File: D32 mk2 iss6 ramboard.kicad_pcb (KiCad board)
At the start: 2 copper layers, 117.5 x 53.3 mm, 34 parts, among them IC1 4116, IC2 4116, IC3 4116, IC36 4116, IC37 4116, IC38 4116, IC39 4116, IC4 4116, IC40 4116, IC41 4116, IC42 4116, IC43 4116, IC5 4116, IC6 4116, IC7 4116, IC8 4116, U1 4164, U10 4164, U11 4164, U12 4164, U13 4164, U14 4164, U15 4164, U16 4164, U2 4164, U3 4164, U4 4164, U5 4164, U6 4164, U7 4164, U8 4164, U9 4164

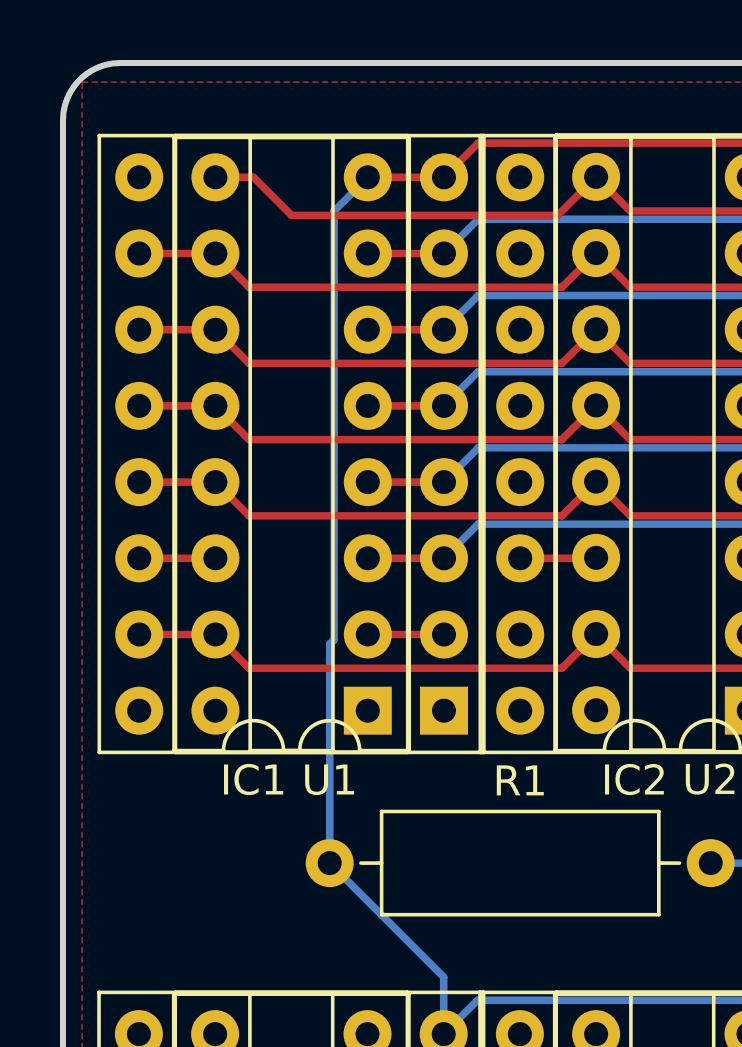
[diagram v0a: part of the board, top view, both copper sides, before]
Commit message: fix 4116 pin bindings
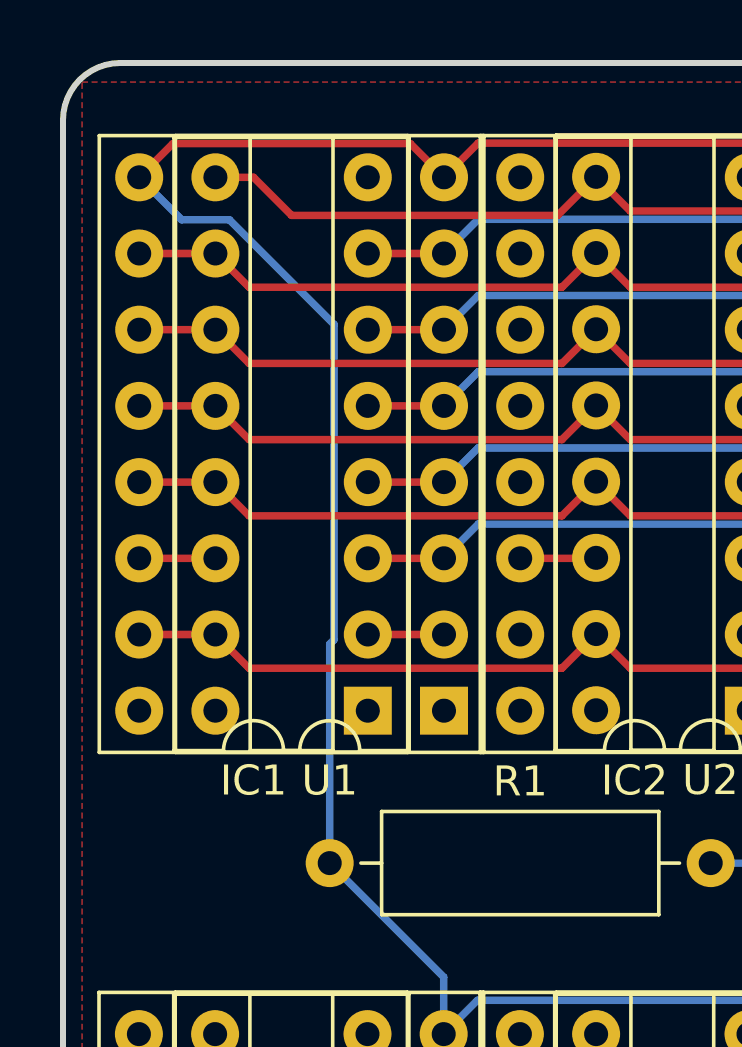
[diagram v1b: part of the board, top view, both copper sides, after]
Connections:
- IC1 pad 8: +5V -> unconnected-(IC1-Pad8)
- IC1 pad 9: unconnected-(IC1-Pad9) -> +5V
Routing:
- net +5V: track 224.2 -> 235.9 mm

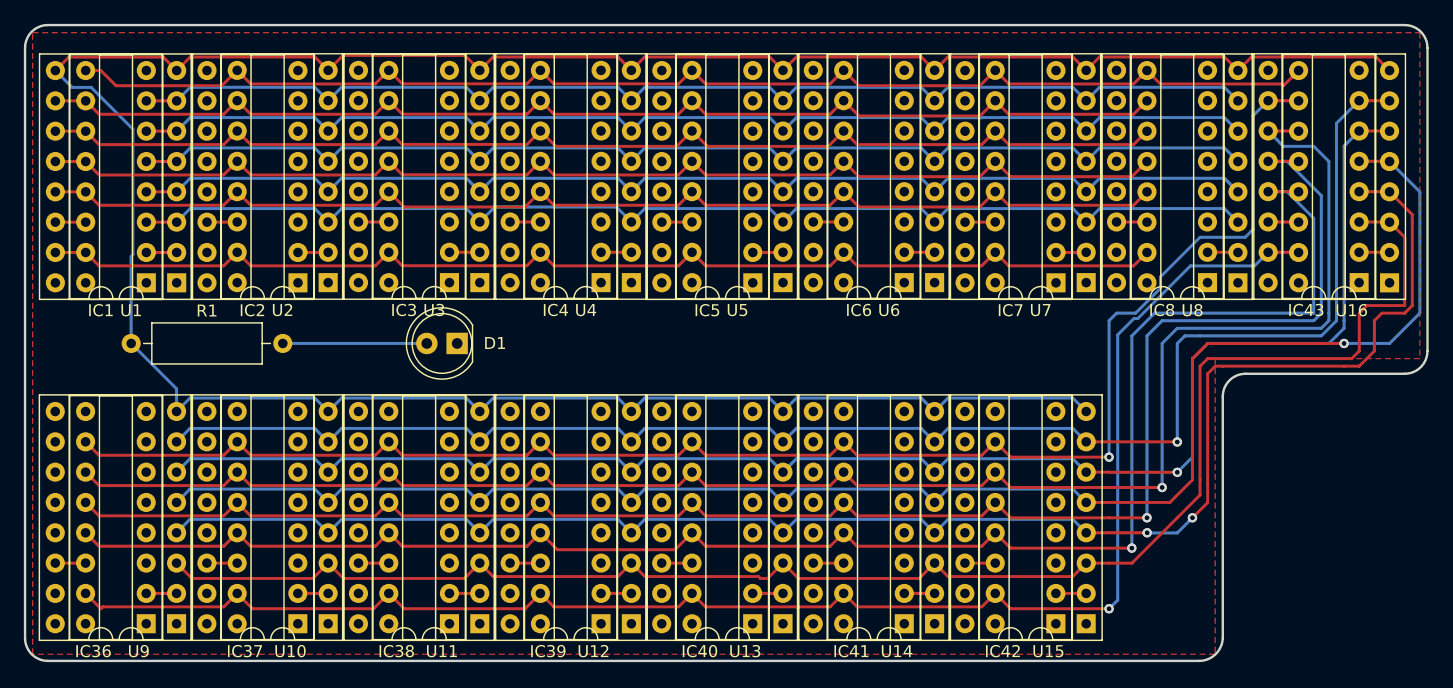
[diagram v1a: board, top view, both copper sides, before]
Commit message: correct 4116 pins and simplify networks
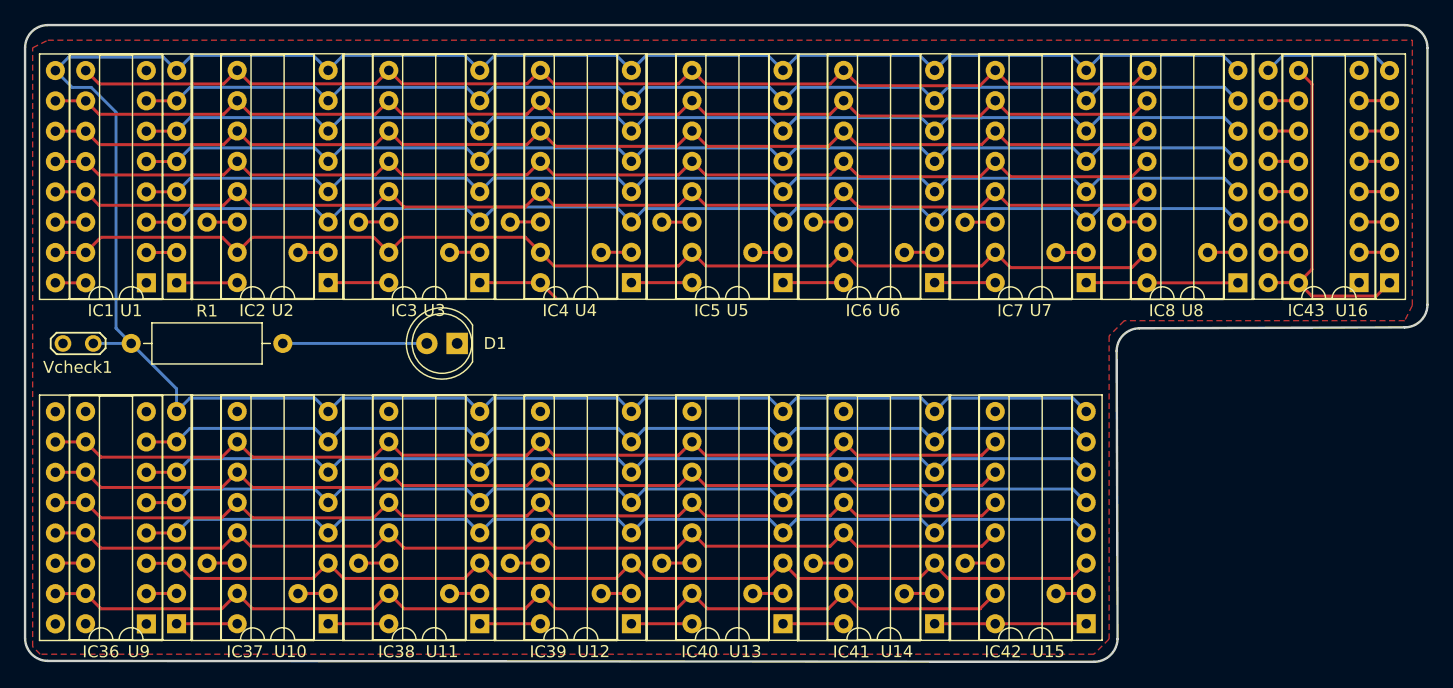
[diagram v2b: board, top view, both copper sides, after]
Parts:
- added Vcheck1: TestPoint_2Pole, TestPoint:TestPoint_2Pads_Pitch2.54mm_Drill0.8mm, F.Cu at (92.1, 91.4)
- IC2, IC3, IC37, IC38, IC39, IC4, IC40, IC41, IC42, IC5, IC6, IC7, IC8: footprint Package_DIP:DIP-16_W7.62mm_Socket -> 4116:4116_Min_DIP-16_W7.62mm_Socket
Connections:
- IC36 pad 10: unconnected-(IC36-Pad10) -> Net-(IC36-Pad10)
- IC36 pad 11: unconnected-(IC36-Pad11) -> Net-(IC36-Pad11)
- IC36 pad 12: unconnected-(IC36-Pad12) -> Net-(IC36-Pad12)
- IC36 pad 13: unconnected-(IC36-Pad13) -> Net-(IC36-Pad13)
- IC36 pad 15: unconnected-(IC36-Pad15) -> Net-(IC36-Pad15)
- IC36 pad 3: unconnected-(IC36-Pad3) -> Net-(IC36-Pad3)
- IC36 pad 4: unconnected-(IC36-Pad4) -> Net-(IC36-Pad4)
- IC36 pad 5: unconnected-(IC36-Pad5) -> Net-(IC36-Pad5)
- IC36 pad 6: unconnected-(IC36-Pad6) -> Net-(IC36-Pad6)
- IC36 pad 7: unconnected-(IC36-Pad7) -> Net-(IC36-Pad7)
- IC43 pad 16: GND -> Net-(IC43-Pad16)
- IC43 pad 9: unconnected-(IC43-Pad9) -> Net-(IC43-Pad9)
- U1 pad 1: unconnected-(U1-Pad1) -> GND
- U10 pad 1: unconnected-(U10-Pad1) -> GND
- U10 pad 10: Net-(IC43-Pad10) -> Net-(IC36-Pad10)
- U10 pad 11: Net-(IC43-Pad11) -> Net-(IC36-Pad11)
- U10 pad 12: Net-(IC43-Pad12) -> Net-(IC36-Pad12)
- U10 pad 13: Net-(IC43-Pad13) -> Net-(IC36-Pad13)
- U10 pad 15: Net-(IC43-Pad15) -> Net-(IC36-Pad15)
- U10 pad 3: Net-(IC43-Pad3) -> Net-(IC36-Pad3)
- U10 pad 4: Net-(IC43-Pad4) -> Net-(IC36-Pad4)
- U10 pad 5: Net-(IC43-Pad5) -> Net-(IC36-Pad5)
- U10 pad 6: Net-(IC43-Pad6) -> Net-(IC36-Pad6)
- U10 pad 7: Net-(IC43-Pad7) -> Net-(IC36-Pad7)
- U11 pad 1: unconnected-(U11-Pad1) -> GND
- U11 pad 10: Net-(IC43-Pad10) -> Net-(IC36-Pad10)
- U11 pad 11: Net-(IC43-Pad11) -> Net-(IC36-Pad11)
- U11 pad 12: Net-(IC43-Pad12) -> Net-(IC36-Pad12)
- U11 pad 13: Net-(IC43-Pad13) -> Net-(IC36-Pad13)
- U11 pad 15: Net-(IC43-Pad15) -> Net-(IC36-Pad15)
- U11 pad 3: Net-(IC43-Pad3) -> Net-(IC36-Pad3)
- U11 pad 4: Net-(IC43-Pad4) -> Net-(IC36-Pad4)
- U11 pad 5: Net-(IC43-Pad5) -> Net-(IC36-Pad5)
- U11 pad 6: Net-(IC43-Pad6) -> Net-(IC36-Pad6)
- U11 pad 7: Net-(IC43-Pad7) -> Net-(IC36-Pad7)
- U12 pad 1: unconnected-(U12-Pad1) -> GND
- U12 pad 10: Net-(IC43-Pad10) -> Net-(IC36-Pad10)
- U12 pad 11: Net-(IC43-Pad11) -> Net-(IC36-Pad11)
- U12 pad 12: Net-(IC43-Pad12) -> Net-(IC36-Pad12)
- U12 pad 13: Net-(IC43-Pad13) -> Net-(IC36-Pad13)
- U12 pad 15: Net-(IC43-Pad15) -> Net-(IC36-Pad15)
- U12 pad 3: Net-(IC43-Pad3) -> Net-(IC36-Pad3)
- U12 pad 4: Net-(IC43-Pad4) -> Net-(IC36-Pad4)
- U12 pad 5: Net-(IC43-Pad5) -> Net-(IC36-Pad5)
- U12 pad 6: Net-(IC43-Pad6) -> Net-(IC36-Pad6)
- U12 pad 7: Net-(IC43-Pad7) -> Net-(IC36-Pad7)
- U13 pad 1: unconnected-(U13-Pad1) -> GND
- U13 pad 10: Net-(IC43-Pad10) -> Net-(IC36-Pad10)
- U13 pad 11: Net-(IC43-Pad11) -> Net-(IC36-Pad11)
- U13 pad 12: Net-(IC43-Pad12) -> Net-(IC36-Pad12)
- U13 pad 13: Net-(IC43-Pad13) -> Net-(IC36-Pad13)
- U13 pad 15: Net-(IC43-Pad15) -> Net-(IC36-Pad15)
- U13 pad 3: Net-(IC43-Pad3) -> Net-(IC36-Pad3)
- U13 pad 4: Net-(IC43-Pad4) -> Net-(IC36-Pad4)
- U13 pad 5: Net-(IC43-Pad5) -> Net-(IC36-Pad5)
- U13 pad 6: Net-(IC43-Pad6) -> Net-(IC36-Pad6)
- U13 pad 7: Net-(IC43-Pad7) -> Net-(IC36-Pad7)
- U14 pad 1: unconnected-(U14-Pad1) -> GND
- U14 pad 10: Net-(IC43-Pad10) -> Net-(IC36-Pad10)
- U14 pad 11: Net-(IC43-Pad11) -> Net-(IC36-Pad11)
- U14 pad 12: Net-(IC43-Pad12) -> Net-(IC36-Pad12)
- U14 pad 13: Net-(IC43-Pad13) -> Net-(IC36-Pad13)
- U14 pad 15: Net-(IC43-Pad15) -> Net-(IC36-Pad15)
- U14 pad 3: Net-(IC43-Pad3) -> Net-(IC36-Pad3)
- U14 pad 4: Net-(IC43-Pad4) -> Net-(IC36-Pad4)
- U14 pad 5: Net-(IC43-Pad5) -> Net-(IC36-Pad5)
- U14 pad 6: Net-(IC43-Pad6) -> Net-(IC36-Pad6)
- U14 pad 7: Net-(IC43-Pad7) -> Net-(IC36-Pad7)
- U15 pad 1: unconnected-(U15-Pad1) -> GND
- U15 pad 10: Net-(IC43-Pad10) -> Net-(IC36-Pad10)
- U15 pad 11: Net-(IC43-Pad11) -> Net-(IC36-Pad11)
- U15 pad 12: Net-(IC43-Pad12) -> Net-(IC36-Pad12)
- U15 pad 13: Net-(IC43-Pad13) -> Net-(IC36-Pad13)
- U15 pad 15: Net-(IC43-Pad15) -> Net-(IC36-Pad15)
- U15 pad 3: Net-(IC43-Pad3) -> Net-(IC36-Pad3)
- U15 pad 4: Net-(IC43-Pad4) -> Net-(IC36-Pad4)
- U15 pad 5: Net-(IC43-Pad5) -> Net-(IC36-Pad5)
- U15 pad 6: Net-(IC43-Pad6) -> Net-(IC36-Pad6)
- U15 pad 7: Net-(IC43-Pad7) -> Net-(IC36-Pad7)
- U16 pad 1: unconnected-(U16-Pad1) -> Net-(IC43-Pad16)
- U16 pad 16: GND -> Net-(IC43-Pad16)
- U16 pad 8: +5V -> Net-(IC43-Pad9)
- U16 pad 9: GND -> Net-(IC43-Pad16)
- U2 pad 1: unconnected-(U2-Pad1) -> GND
- U3 pad 1: unconnected-(U3-Pad1) -> GND
- U4 pad 1: unconnected-(U4-Pad1) -> GND
- U5 pad 1: unconnected-(U5-Pad1) -> GND
- U6 pad 1: unconnected-(U6-Pad1) -> GND
- U7 pad 1: unconnected-(U7-Pad1) -> GND
- U8 pad 1: unconnected-(U8-Pad1) -> GND
- U9 pad 1: unconnected-(U9-Pad1) -> GND
- U9 pad 10: Net-(IC43-Pad10) -> Net-(IC36-Pad10)
- U9 pad 11: Net-(IC43-Pad11) -> Net-(IC36-Pad11)
- U9 pad 12: Net-(IC43-Pad12) -> Net-(IC36-Pad12)
- U9 pad 13: Net-(IC43-Pad13) -> Net-(IC36-Pad13)
- U9 pad 15: Net-(IC43-Pad15) -> Net-(IC36-Pad15)
- U9 pad 3: Net-(IC43-Pad3) -> Net-(IC36-Pad3)
- U9 pad 4: Net-(IC43-Pad4) -> Net-(IC36-Pad4)
- U9 pad 5: Net-(IC43-Pad5) -> Net-(IC36-Pad5)
- U9 pad 6: Net-(IC43-Pad6) -> Net-(IC36-Pad6)
- U9 pad 7: Net-(IC43-Pad7) -> Net-(IC36-Pad7)
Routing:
- net Net-(IC43-Pad11): track 145.2 -> 2.56 mm, vias 1 -> 0
- net Net-(IC43-Pad12): track 143.7 -> 2.56 mm, vias 1 -> 0
- net Net-(IC43-Pad13): track 143.1 -> 2.56 mm, vias 1 -> 0
- net Net-(IC43-Pad5): track 138.6 -> 2.56 mm, vias 1 -> 0
- net Net-(IC43-Pad4): track 137.7 -> 2.56 mm, vias 2 -> 0
- net Net-(IC43-Pad3): track 136.2 -> 2.56 mm
- net Net-(IC43-Pad7): track 133.6 -> 2.56 mm, vias 1 -> 0
- net Net-(IC43-Pad15): track 133.6 -> 2.56 mm, vias 1 -> 0
- net Net-(IC43-Pad10): track 132.9 -> 2.56 mm, vias 1 -> 0
- net Net-(IC43-Pad6): track 132.8 -> 2.56 mm, vias 1 -> 0
- net Net-(IC36-Pad3): track 0.00 -> 85.2 mm
- net Net-(IC36-Pad15): track 0.00 -> 85.2 mm
- net Net-(IC36-Pad13): track 0.00 -> 84.7 mm
- net Net-(IC36-Pad11): track 0.00 -> 84.6 mm
- net Net-(IC36-Pad10): track 0.00 -> 84.6 mm
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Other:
- outline, holes or cut-outs redrawn
- board text added: "Created by Julian Brown"
- board text added: "Dragon 32 Mk2 Issue 6 Ram Repair"
- board text added: "Revision 1"
